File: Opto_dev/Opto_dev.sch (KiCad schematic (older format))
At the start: 2 parts

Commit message: Added schematics
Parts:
- removed R?: R, symbol Device:R
- removed U?: LM386, symbol Amplifier_Audio:LM386
- added C1: C, symbol Device:C
- added C2: 220nF, symbol Device:C
- added D1: LED, symbol Device:LED
- added D2: 1N4007, Diode_THT:D_DO-41_SOD81_P10.16mm_Horizontal, symbol Diode:1N4007
- added L1: 10u, symbol Device:L
- added Q1, Q2: IRLZ44N, Package_TO_SOT_THT:TO-220-3_Vertical, symbol Transistor_FET:IRLZ44N
- added R1: 10k, symbol Device:R
- added R2: 1k, symbol Device:R
- added R3: 1, symbol Device:R
- added R4, R5: 10, symbol Device:R
- added R6: R, symbol Device:R
- added R7: 5.1k, symbol Device:R
- added U1, U4: MCP602, symbol pspice:OPAMP
- added U2, U3: TC4421, Package_DIP:DIP-8-N6_W7.62mm, symbol Driver_FET:TC4421
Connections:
- new net: Q2.1 (G), R5.2
- new net: Q2.2 (D), R3.2
- new net: R5.1, U3.6 (~OUTPUT), U3.7 (~OUTPUT)
- new net: D1.1 (K), D2.1 (K), L1.1
- new net: D2.2 (A), L1.2, Q1.2 (D)
- new net: Q1.1 (G), R4.2
- new net: Q1.3 (S), R3.1, U1.1 (+)
- new net: R4.1, U2.6 (~OUTPUT), U2.7 (~OUTPUT)
- new net: U2.2 (INPUT), U4.3
- new net: R1.2, R2.1, U1.2 (-)
- new net: R1.1, U1.3, U4.2 (-)
- new net +5V: U1.4 (V+), U4.4 (V+)
- new net ANALOG_INPUT: C2.1, R7.2, U4.1 (+)
- new net GND: C2.2, Q2.3 (S), R2.2, U1.5 (V-), U2.4 (GND), U2.5 (GND), U3.4 (GND), U3.5 (GND), U4.5 (V-)
- new net LED_ENABLE: U3.2 (INPUT)
- new net PWM_INPUT: R7.1
- new net VCC: D1.2 (A), U2.1 (VDD), U2.8 (VDD), U3.1 (VDD), U3.8 (VDD)

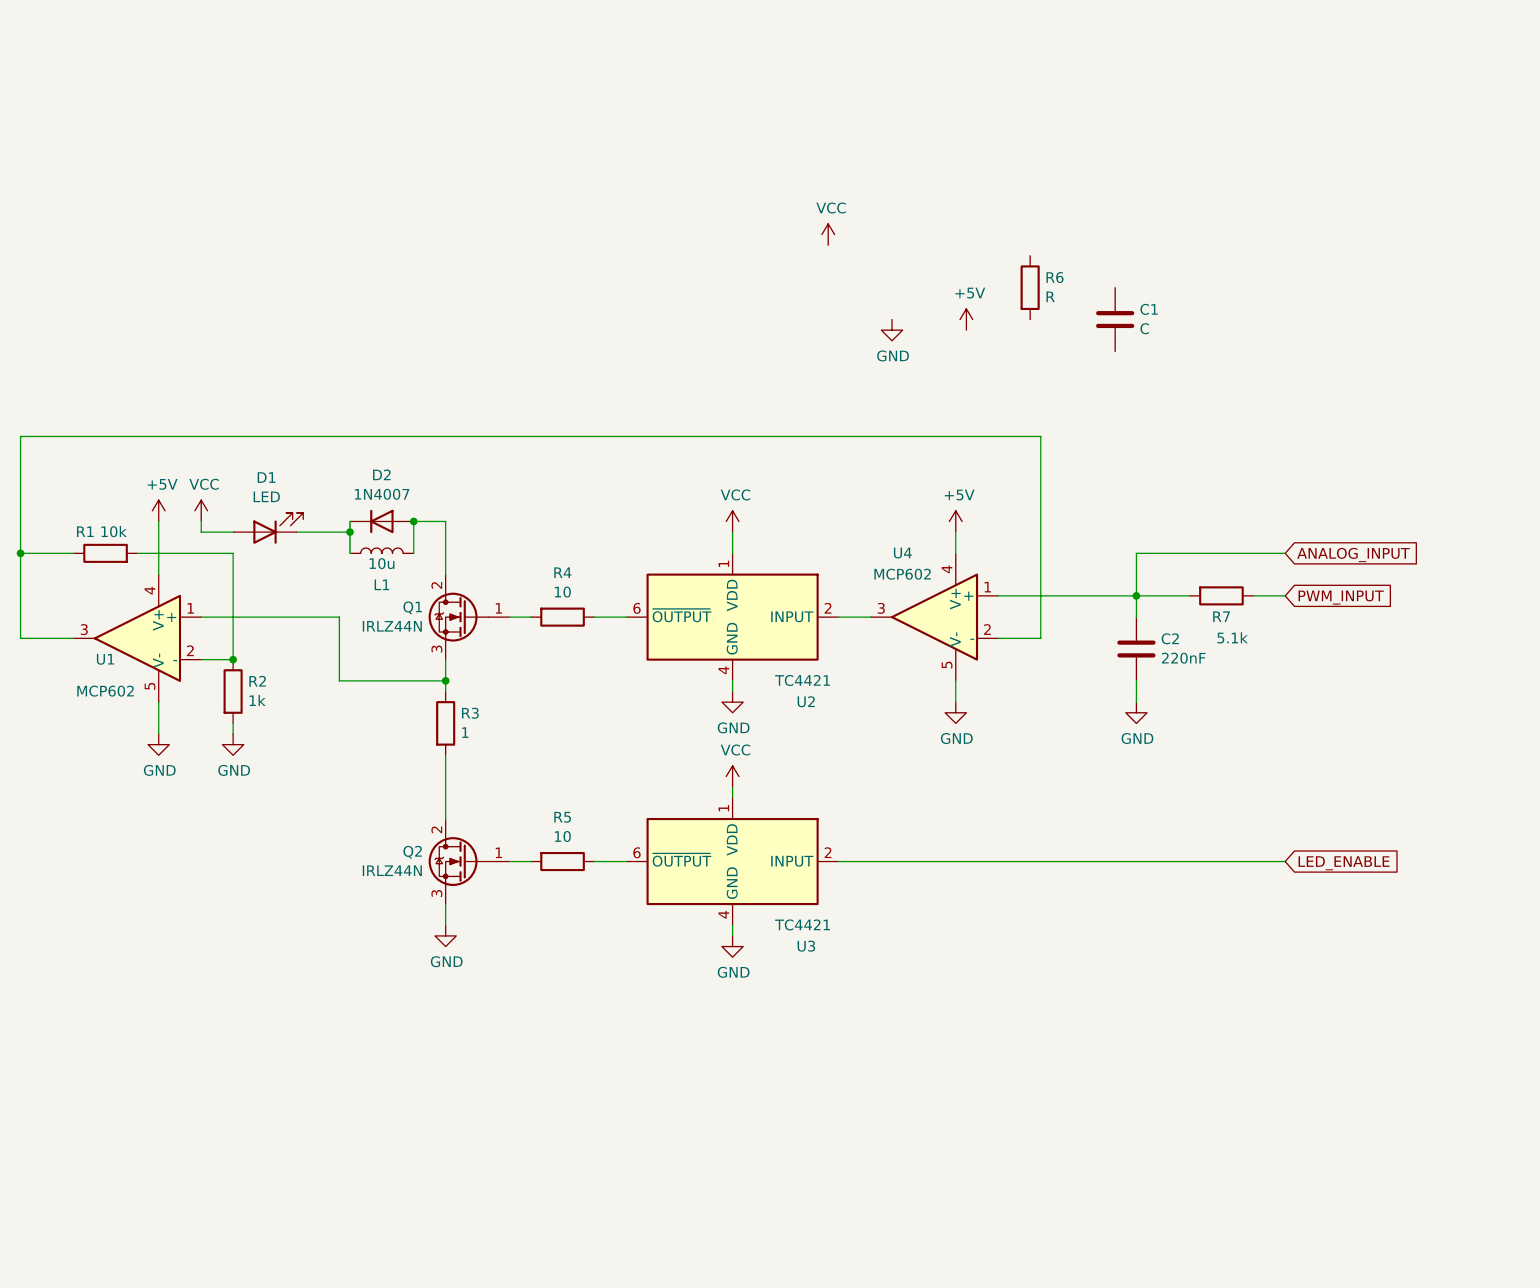
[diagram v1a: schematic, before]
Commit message: added code vith perfboard layout
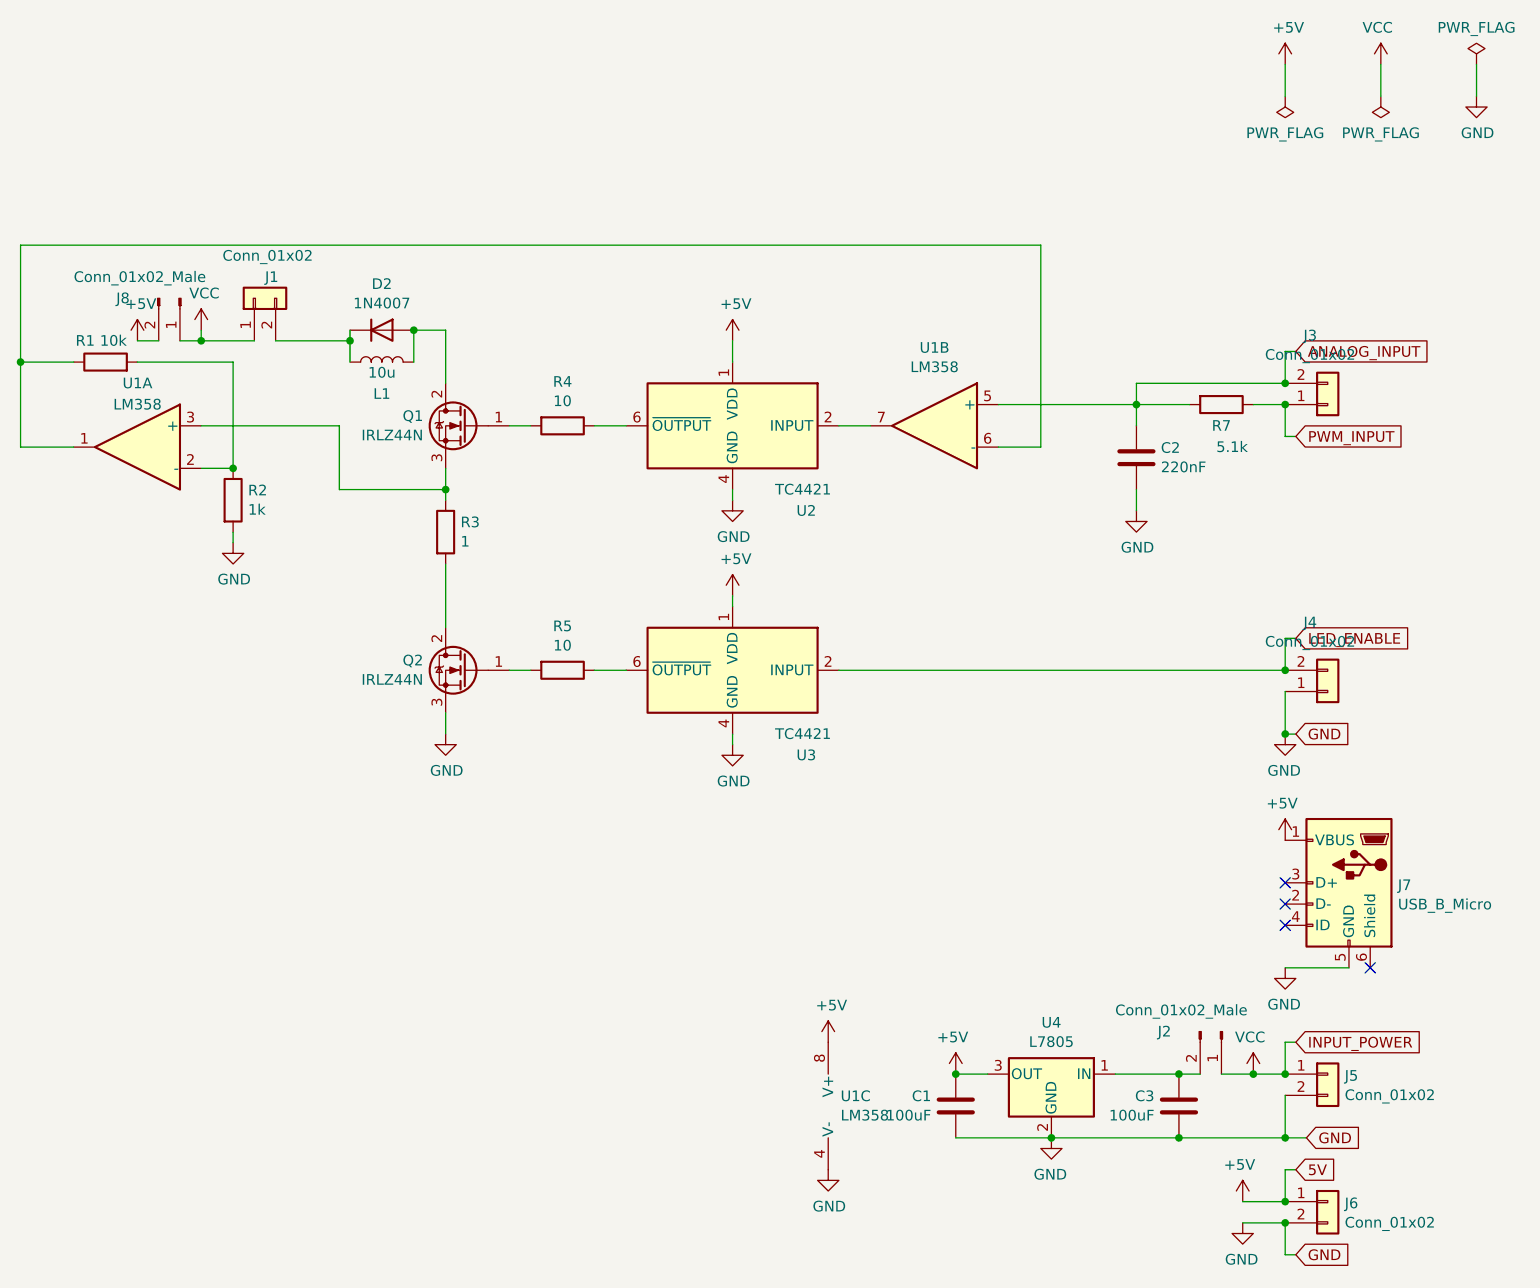
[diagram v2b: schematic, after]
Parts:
- removed D1: LED, symbol Device:LED
- removed R6: R, symbol Device:R
- removed U1, U4: MCP602, symbol pspice:OPAMP
- added C3: 100uF, Capacitor_THT:CP_Radial_D6.3mm_P2.50mm, symbol Device:C
- added J1, J3, J4, J5, J6: Conn_01x02, TerminalBlock:TerminalBlock_bornier-2_P5.08mm, symbol Connector_Generic:Conn_01x02
- added J2, J8: Conn_01x02_Male, Connector_PinHeader_2.54mm:PinHeader_1x02_P2.54mm_Vertical, symbol Connector:Conn_01x02_Male
- added J7: USB_B_Micro, Connector_PinHeader_2.54mm:PinHeader_1x05_P2.54mm_Vertical, symbol Connector:USB_B_Micro
- added U1: LM358, Package_DIP:DIP-8_W7.62mm_Socket_LongPads, symbol Amplifier_Operational:LM358
- added U4: L7805, Package_TO_SOT_THT:TO-220-3_Vertical, symbol Regulator_Linear:L7805
- C1: value C -> 100uF; footprint (none) -> Capacitor_THT:CP_Radial_D6.3mm_P2.50mm
- C2: footprint (none) -> Capacitor_THT:C_Disc_D4.7mm_W2.5mm_P5.00mm
- L1: footprint (none) -> Inductor_THT:L_Radial_D9.5mm_P5.00mm_Fastron_07HVP
- R1, R2, R4, R5, R7: footprint (none) -> Resistor_THT:R_Axial_DIN0204_L3.6mm_D1.6mm_P7.62mm_Horizontal
- R3: footprint (none) -> Resistor_THT:R_Axial_DIN0918_L18.0mm_D9.0mm_P22.86mm_Horizontal
- U2, U3: footprint Package_DIP:DIP-8-N6_W7.62mm -> Package_DIP:DIP-8_W7.62mm_Socket_LongPads
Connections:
- net +5V: now also C1.1, U2.1 (VDD), U2.8 (VDD), U3.1 (VDD), U3.8 (VDD), J6.1 (Pin_1), J7.1 (VBUS), J8.2 (Pin_2), U1.8 (V+), U4.3 (OUT)
- net ANALOG_INPUT: now also J3.2 (Pin_2), U1.5 (+)
- net GND: now also C1.2, C3.2, J4.1 (Pin_1), J5.2 (Pin_2), J6.2 (Pin_2), J7.5 (GND), U1.4 (V-), U4.2 (GND)
- net LED_ENABLE: now also J4.2 (Pin_2)
- net PWM_INPUT: now also J3.1 (Pin_1)
- net VCC: now also J1.1 (Pin_1), J2.1 (Pin_1), J5.1 (Pin_1), J8.1 (Pin_1); no longer U2.1 (VDD), U2.8 (VDD), U3.1 (VDD), U3.8 (VDD)
- net at D2.1 (K), L1.1: now also J1.2 (Pin_2)
- net at Q1.3 (S), R3.1: now also U1.3 (+)
- net at U2.2 (INPUT): now also U1.7
- net at R1.2, R2.1: now also U1.2 (-)
- net at R1.1: now also U1.1, U1.6 (-)
- new net: C3.1, J2.2 (Pin_2), U4.1 (IN)
- no-connect marks 0 -> 4
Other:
- moved on the sheet: C2, D2, L1, Q1, Q2, R1, R2, R3, R4, R5, R7, U2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
